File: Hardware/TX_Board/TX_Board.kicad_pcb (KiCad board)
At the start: 2 copper layers, 148 x 98.8 mm, 224 parts, among them IC1 GP2Y1+, IC10 QPA9122TR7, IC11 MAPS-010164-TR0500, IC12 QPA9122TR7, IC13 MAPS-010164-TR0500, IC14 QPA9122TR7, IC2 GP2Y1+, IC3 GP2Y1+, IC4 LT3041ADE#PBF, IC5 LT3099ADE#PBF, IC6 ADPL40502AUJZ-1.5-R7, IC7 MAPS-010164-TR0500, IC8 QPA9122TR7, IC9 MAPS-010164-TR0500, J1 Conn_Coaxial, J10 MM8030-2610RJ3, J11 MM8030-2610RJ3, J12 MM8030-2610RJ3, J13 MM8030-2610RJ3, J14 MM8030-2610RJ3, J15 Conn_Coaxial, J16 MM8030-2610RJ3, J17 MM8030-2610RJ3, J18 Conn_Coaxial, J19 MM8030-2610RJ3, J2 Conn_01x01_Pin, J20 MM8030-2610RJ3, J21 Conn_Coaxial, J22 MM8030-2610RJ3, J23 MM8030-2610RJ3, J24 Conn_Coaxial, J3 Conn_01x01_Pin, J4 Conn_01x01_Pin, J5 Conn_01x01_Pin, J6 Conn_02x12_Odd_Even, J7 Conn_01x03_Socket, J8 Conn_02x08_Odd_Even, J9 MM8030-2610RJ3, U1 SN74HCT138NSR

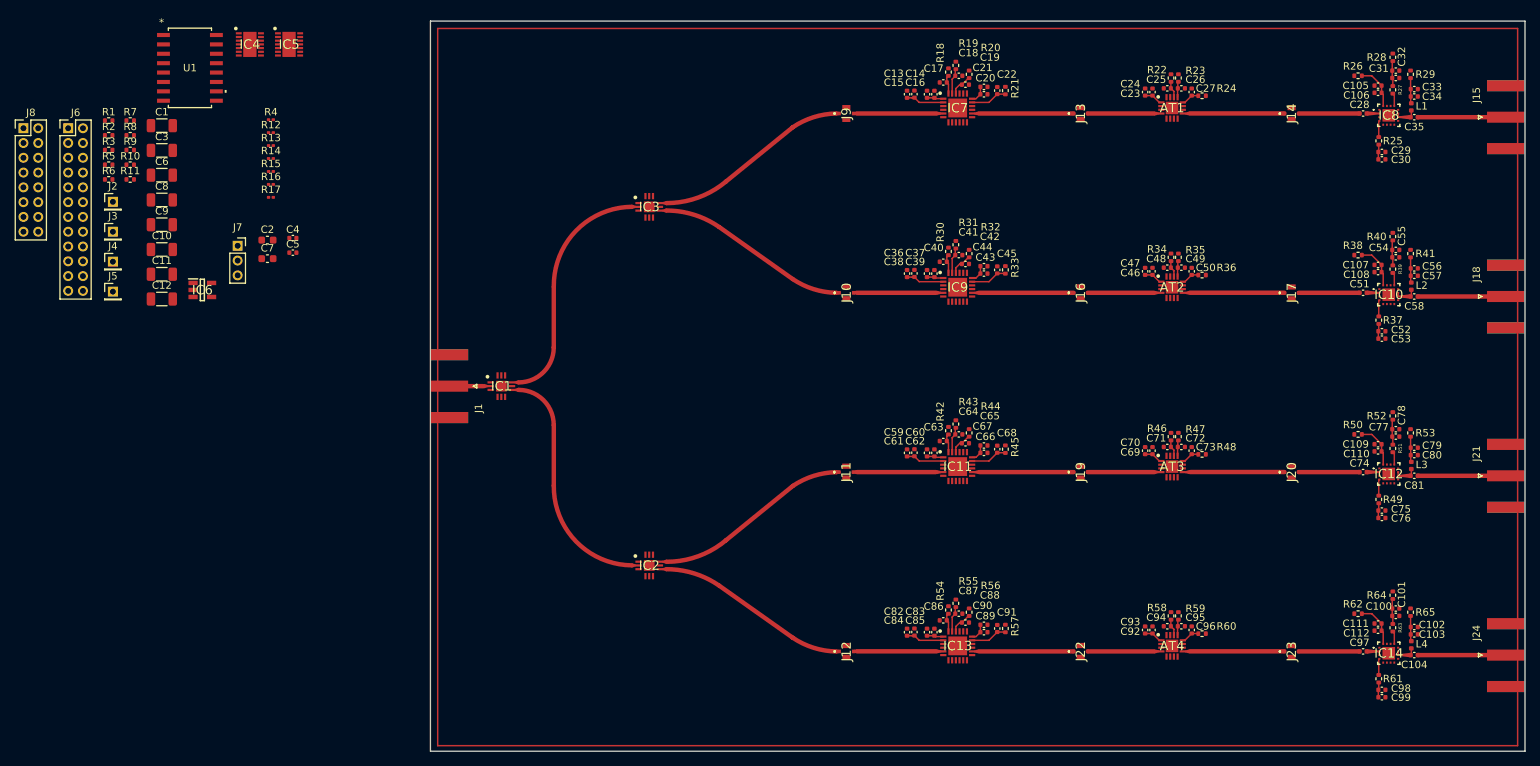
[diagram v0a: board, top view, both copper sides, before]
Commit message: Shrinking layout
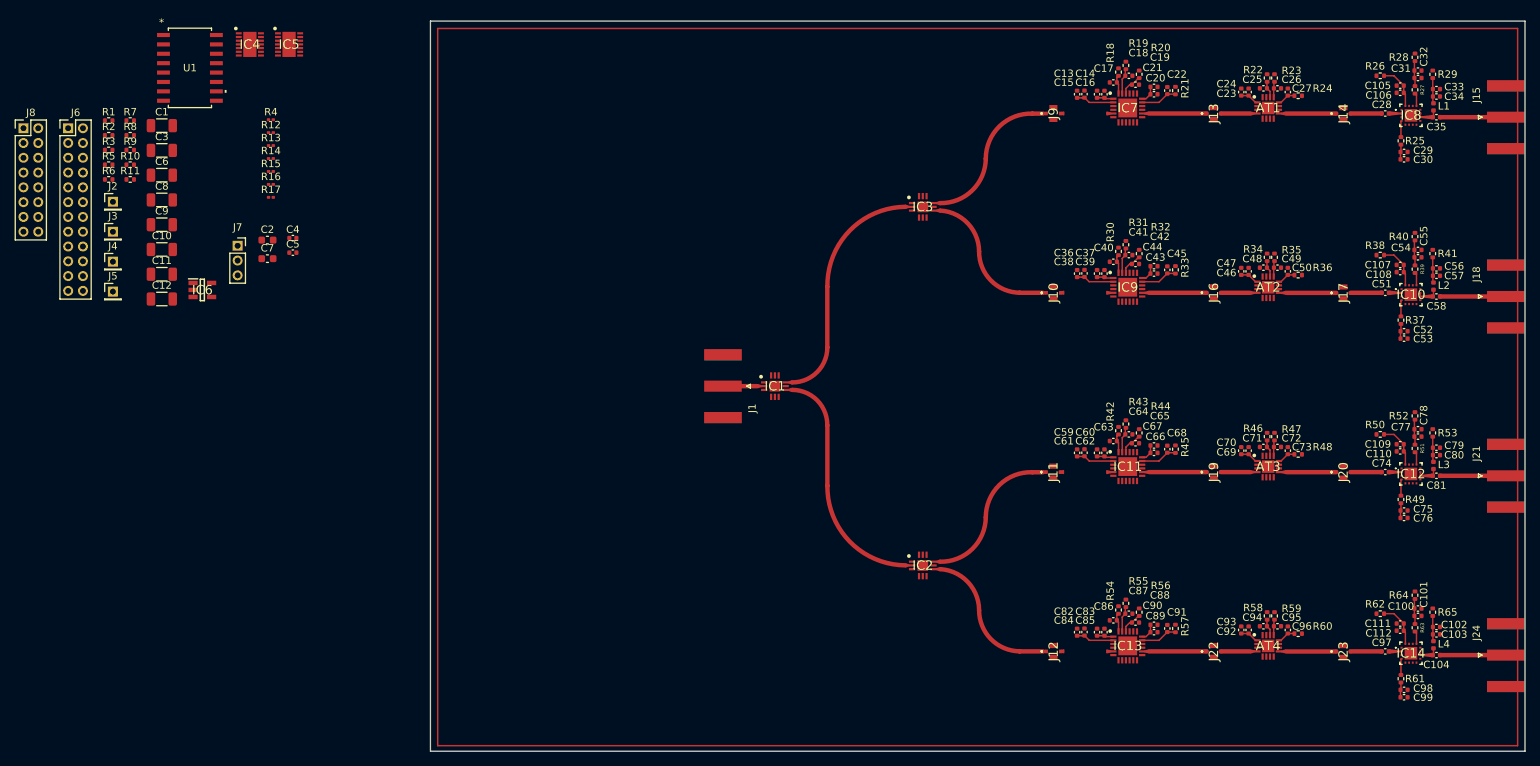
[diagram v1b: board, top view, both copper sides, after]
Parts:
- moved IC1 37.0 mm to (128.6, 79.4)
- moved IC2 37.0 mm to (148.6, 103.6)
- moved IC3 37.0 mm to (148.6, 55.1)
- moved J1 37.0 mm to (121.5, 79.4)
- moved J10 28.0 mm to (166.2, 66.8)
- moved J11 28.0 mm to (166.2, 91.0)
- moved J12 28.0 mm to (166.2, 115.3)
- moved J9 28.0 mm to (166.2, 42.5)
- moved C13 23.0 mm to (169.4, 39.9)
- moved C14 23.0 mm to (172.1, 39.9)
- moved C15 23.0 mm to (170.4, 39.9)
- moved C16 23.0 mm to (173.1, 39.9)
- moved C17 23.0 mm to (174.3, 38.3)
- moved C18 23.0 mm to (176.4, 37.4)
- moved C19 23.0 mm to (177.3, 38.6)
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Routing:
- net RF_IN4: track 11.6 -> 0.00 mm
- net RF_IN1: track 11.6 -> 0.00 mm
- net RF_IN3: track 11.6 -> 0.00 mm
- net RF_IN2: track 11.6 -> 0.00 mm
- net Net-(AT4-RFOUT): track 12.8 -> 6.72 mm
- net Net-(AT3-RFOUT): track 12.8 -> 6.72 mm
- net Net-(AT2-RFOUT): track 12.8 -> 6.72 mm
- net Net-(AT1-RFOUT): track 12.8 -> 6.72 mm
- net Net-(IC9-RF_OUT): track 12.7 -> 7.72 mm
- net Net-(IC7-RF_OUT): track 12.7 -> 7.72 mm
- net Net-(IC13-RF_OUT): track 12.7 -> 7.72 mm
- net Net-(IC11-RF_OUT): track 12.7 -> 7.72 mm
- net Net-(AT4-RFIN): track 8.92 -> 3.92 mm
- net Net-(AT3-RFIN): track 8.92 -> 3.92 mm
- net Net-(AT2-RFIN): track 8.92 -> 3.92 mm
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
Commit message: prelim power/logic placement
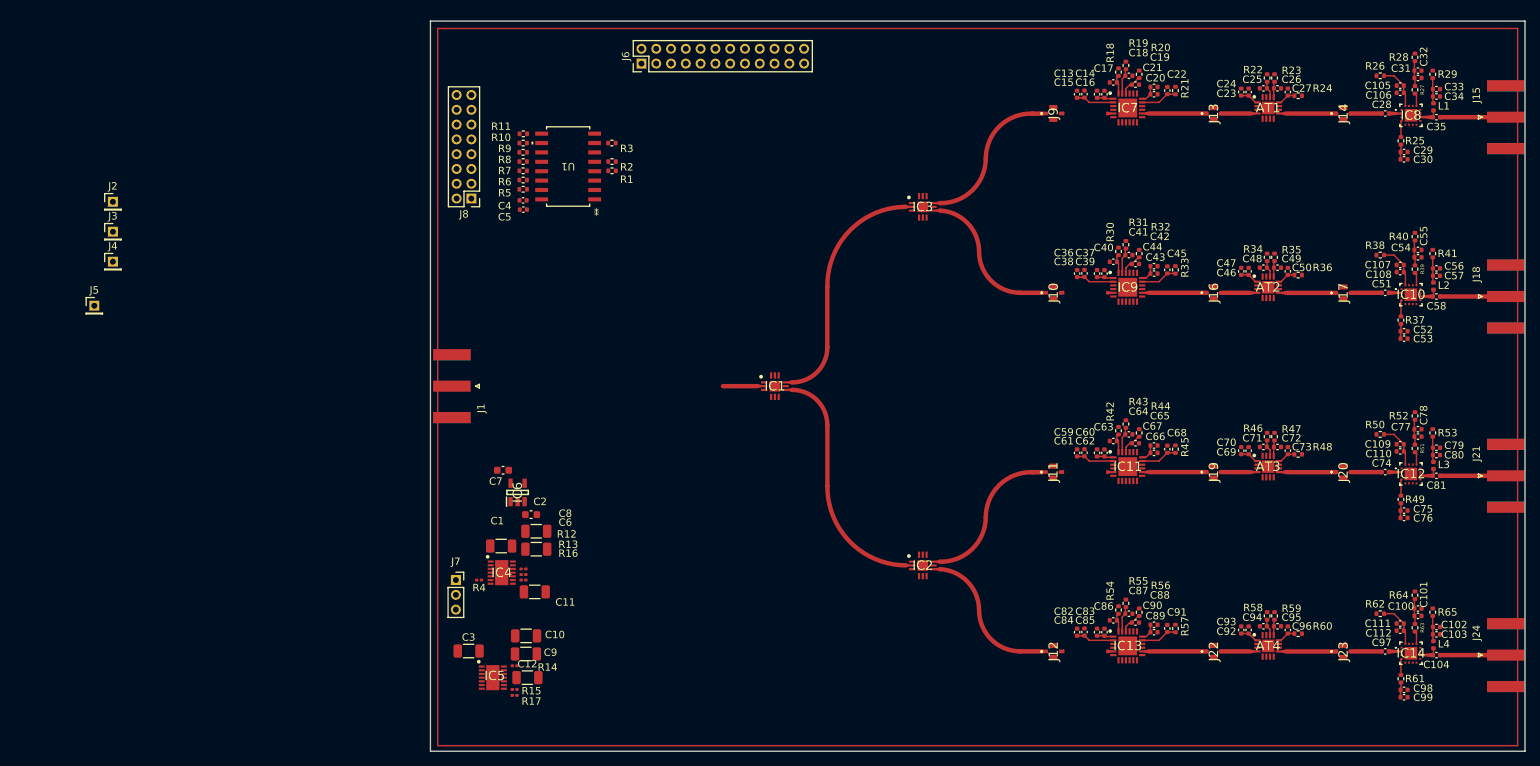
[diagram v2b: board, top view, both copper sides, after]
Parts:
- moved IC5 90.0 mm to (90.4, 118.8)
- moved C3 79.4 mm to (87.1, 115.2)
- moved IC4 79.1 mm to (91.6, 104.6)
- moved R15 78.2 mm to (93.3, 121.2)
- moved J6 78.0 mm to (110.5, 35.8), turned to 90 degrees
- moved C9 76.1 mm to (94.9, 115.6), turned to 180 degrees
- moved R14 76.1 mm to (93.3, 117.2)
- moved R17 74.3 mm to (93.3, 120.4), turned to 180 degrees
- moved C1 73.1 mm to (91.5, 101.0), turned to 180 degrees
- moved C10 71.8 mm to (94.9, 113.2), turned to 180 degrees
- moved C6 71.6 mm to (96.3, 101.4), turned to 180 degrees
- moved C12 71.2 mm to (95.1, 118.8)
- moved R1 68.4 mm to (106.5, 50.2), turned to 180 degrees
- moved R4 68.3 mm to (88.5, 105.6), turned to 180 degrees
- moved R12 68.2 mm to (94.5, 104.1)
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
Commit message: Waveguide + ground planes and P.S. daughter board modification
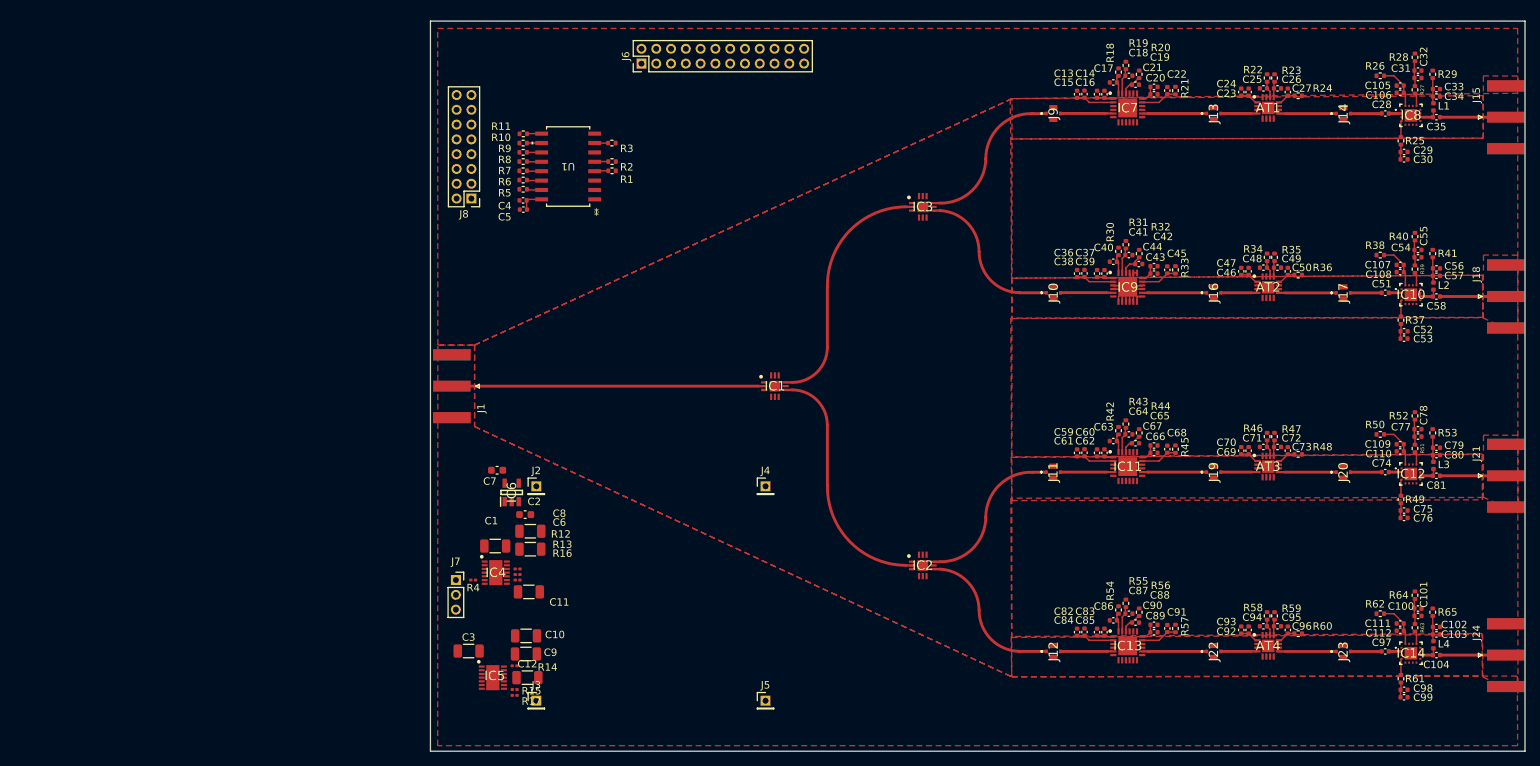
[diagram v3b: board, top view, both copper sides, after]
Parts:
- moved J5 105.3 mm to (127.3, 121.9)
- moved J4 93.3 mm to (127.3, 92.9)
- moved J3 85.5 mm to (96.3, 121.9)
- moved J2 69.0 mm to (96.3, 92.9)
- moved C1 0.80 mm to (90.7, 101.0)
- moved C6 0.80 mm to (95.5, 101.4)
- moved C7 0.80 mm to (91.0, 90.8)
- moved C8 0.80 mm to (95.5, 99.0)
- moved C11 0.80 mm to (95.3, 107.2)
- moved C2 0.80 mm to (94.8, 96.8)
- moved IC4 0.80 mm to (90.8, 104.6)
- moved IC6 0.80 mm to (93.0, 93.8)
- moved R12 0.80 mm to (93.7, 104.1)
- moved R13 0.80 mm to (93.7, 104.8)
- moved R16 0.80 mm to (93.7, 105.6)
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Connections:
- net Net-(AT1-RFIN) renamed /TX_Channel0/ATTN-RF_IN
- net Net-(AT1-RFOUT) renamed /TX_Channel0/ATTN-RF_OUT
- net Net-(AT2-RFIN) renamed /TX_Channel1/ATTN-RF_IN
- net Net-(AT2-RFOUT) renamed /TX_Channel1/ATTN-RF_OUT
- net Net-(AT3-RFIN) renamed /TX_Channel2/ATTN-RF_IN
- net Net-(AT3-RFOUT) renamed /TX_Channel2/ATTN-RF_OUT
- net Net-(AT4-RFIN) renamed /TX_Channel3/ATTN-RF_IN
- net Net-(AT4-RFOUT) renamed /TX_Channel3/ATTN-RF_OUT
- net Net-(IC1-PORT_1) renamed /IC1-PORT_1
- net Net-(IC1-PORT_2) renamed /IC1-PORT_2
- net Net-(IC1-SUM_PORT) renamed /IC1-SUM_PORT
- net Net-(IC11-RF_OUT) renamed /TX_Channel2/PS-RF_OUT
- net Net-(IC13-RF_OUT) renamed /TX_Channel3/PS-RF_OUT
- net Net-(IC2-PORT_1) renamed /IC2-PORT_1
- net Net-(IC2-PORT_2) renamed /IC2-PORT_2
- net Net-(IC3-PORT_1) renamed /IC3-PORT_1
- net Net-(IC3-PORT_2) renamed /IC3-PORT_2
- net Net-(IC7-RF_OUT) renamed /TX_Channel0/PS-RF_OUT
- net Net-(IC9-RF_OUT) renamed /TX_Channel1/PS-RF_OUT
- net Net-(J14-OUT) renamed /TX_Channel0/AMP-RF_IN
- net Net-(J15-In) renamed /TX_Channel0/AMP-RF_OUT
- net Net-(J17-OUT) renamed /TX_Channel1/AMP-RF_IN
- net Net-(J18-In) renamed /TX_Channel1/AMP-RF_OUT
- net Net-(J20-OUT) renamed /TX_Channel2/AMP-RF_IN
- net Net-(J21-In) renamed /TX_Channel2/AMP-RF_OUT
- net Net-(J23-OUT) renamed /TX_Channel3/AMP-RF_IN
- net Net-(J24-In) renamed /TX_Channel3/AMP-RF_OUT
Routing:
- net /IC1-SUM_PORT: track 4.57 -> 41.4 mm
- net GND: track 0.00 -> 26.6 mm
- net RF_IN4: track 0.00 -> 6.32 mm
- net RF_IN3: track 0.00 -> 6.18 mm
- net RF_IN2: track 0.00 -> 6.02 mm
- net RF_IN1: track 0.00 -> 5.99 mm
- net VCC: track 48.6 -> 52.0 mm
- net Net-(U1-Y0): track 0.00 -> 2.03 mm
- net Net-(U1-Y1): track 0.00 -> 2.02 mm
- net Net-(U1-Y2): track 0.00 -> 2.02 mm
- net Net-(U1-Y3): track 0.00 -> 2.01 mm
- net Net-(U1-Y4): track 0.00 -> 2.00 mm
- net Net-(U1-Y5): track 0.00 -> 2.00 mm
- net Net-(U1-Y6): track 0.00 -> 1.98 mm
- net Net-(U1-*G2A): track 0.00 -> 1.87 mm
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- added copper zone on F.Cu, net GND

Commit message: Ease of construction, added new layers, prelimininary routing.
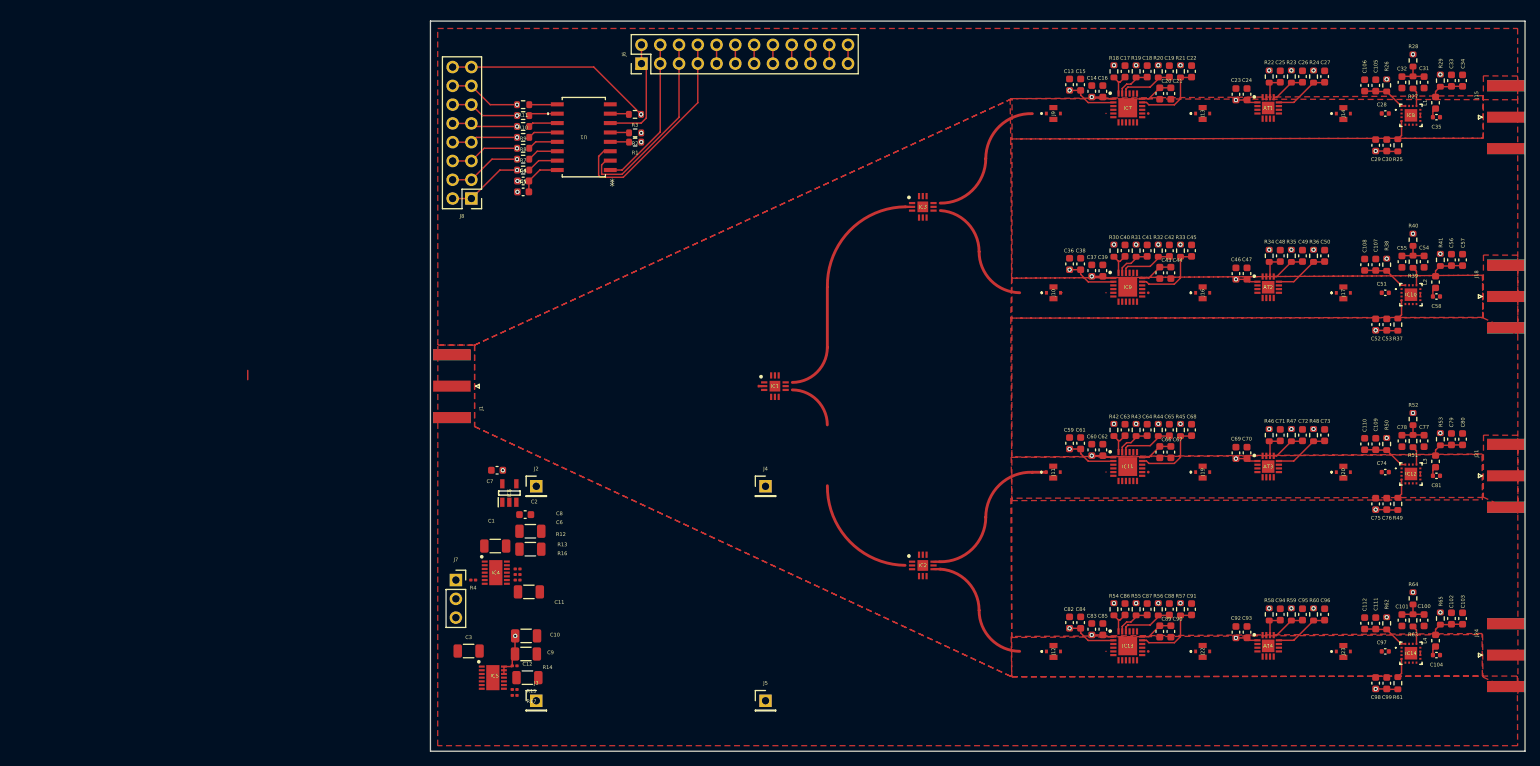
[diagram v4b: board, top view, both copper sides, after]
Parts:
- C100, C101, C102, C103, C105, C106, C107, C108, C109, C110, C111, C112, C13, C14, C15, C16, C17, C18, C19, C20, C21, C22, C23, C24, C25, C26, C27, C29, C30, C31, C32, C33, C34, C36, C37, C38, C39, C4, C40, C41, C42, C43, C44, C45, C46, C47, C48, C49, C5, C50, C52, C53, C54, C55, C56, C57, C59, C60, C61, C62, C63, C64, C65, C66, C67, C68, C69, C70, C71, C72, C73, C75, C76, C77, C78, C79, C80, C82, C83, C84, C85, C86, C87, C88, C89, C90, C91, C92, C93, C94, C95, C96, C98, C99: footprint Capacitor_SMD:C_0402_1005Metric -> Capacitor_SMD:C_0603_1608Metric
- J2, J3, J4, J5: footprint Connector_PinHeader_2.00mm:PinHeader_1x01_P2.00mm_Vertical -> Connector_PinHeader_2.54mm:PinHeader_1x01_P2.54mm_Vertical
- J6: footprint Connector_PinHeader_2.00mm:PinHeader_2x12_P2.00mm_Vertical -> Connector_PinHeader_2.54mm:PinHeader_2x12_P2.54mm_Vertical
- J7: footprint Connector_PinSocket_2.00mm:PinSocket_1x03_P2.00mm_Vertical -> Connector_PinSocket_2.54mm:PinSocket_1x03_P2.54mm_Vertical
- J8: footprint Connector_PinHeader_2.00mm:PinHeader_2x08_P2.00mm_Vertical -> Connector_PinHeader_2.54mm:PinHeader_2x08_P2.54mm_Vertical
- L1, L2, L3, L4: footprint Inductor_SMD:L_0402_1005Metric -> Inductor_SMD:L_0603_1608Metric
- R1, R10, R11, R18, R19, R2, R20, R21, R22, R23, R24, R25, R26, R27, R28, R29, R3, R30, R31, R32, R33, R34, R35, R36, R37, R38, R39, R40, R41, R42, R43, R44, R45, R46, R47, R48, R49, R5, R50, R51, R52, R53, R54, R55, R56, R57, R58, R59, R6, R60, R61, R62, R63, R64, R65, R7, R8, R9: footprint Resistor_SMD:R_0402_1005Metric -> Resistor_SMD:R_0603_1608Metric
- moved C27 5.40 mm to (202.9, 37.5)
- moved C50 5.40 mm to (202.9, 61.8)
- moved C73 5.40 mm to (202.9, 86.0)
- moved C96 5.40 mm to (202.9, 110.2)
- moved R1 4.98 mm to (109.6, 46.4)
- moved R2 4.98 mm to (109.6, 45.1)
- moved R3 4.98 mm to (109.6, 42.6)
- moved C19 4.92 mm to (181.9, 36.8), turned to -90 degrees
- moved C65 4.92 mm to (181.9, 85.3), turned to -90 degrees
- moved C88 4.92 mm to (181.9, 109.5), turned to -90 degrees
- moved C106 4.91 mm to (208.3, 38.7), turned to -90 degrees
- moved C108 4.91 mm to (208.3, 63.0), turned to -90 degrees
- moved C110 4.91 mm to (208.3, 87.2), turned to -90 degrees
- moved C112 4.91 mm to (208.3, 111.5), turned to -90 degrees
- moved C42 4.52 mm to (181.9, 61.0), turned to -90 degrees
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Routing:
- net GPIO3: track 0.00 -> 30.0 mm
- net ATTN_LE_4: track 0.00 -> 28.1 mm, vias 0 -> 2
- net GND: track 26.6 -> 0.00 mm, vias 0 -> 4
- net GPIO2: track 0.00 -> 26.2 mm
- net VCC: track 52.0 -> 76.1 mm, vias 0 -> 20
- net GPIO1: track 0.00 -> 20.7 mm
- net GPIO0: track 0.00 -> 16.4 mm
- net PS_LE_1: track 0.00 -> 10.3 mm, vias 0 -> 2
- net ATTN_LE_1: track 0.00 -> 9.87 mm, vias 0 -> 2
- net PS_LE_4: track 0.00 -> 9.77 mm, vias 0 -> 2
- net VEE: track 9.00 -> 18.4 mm, vias 0 -> 5
- net PS_LE_2: track 0.00 -> 9.43 mm, vias 0 -> 2
- net ATTN_LE_3: track 0.00 -> 9.33 mm, vias 0 -> 2
- net ATTN_LE_2: track 0.00 -> 8.98 mm, vias 0 -> 2
- net PS_LE_3: track 0.00 -> 8.89 mm, vias 0 -> 2
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- added copper zone on In1.Cu, net GND
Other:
- copper layers 2 -> 4
